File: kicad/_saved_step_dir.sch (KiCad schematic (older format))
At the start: 17 parts, among them J1001 tblock2x6, U1001 am26ls32a

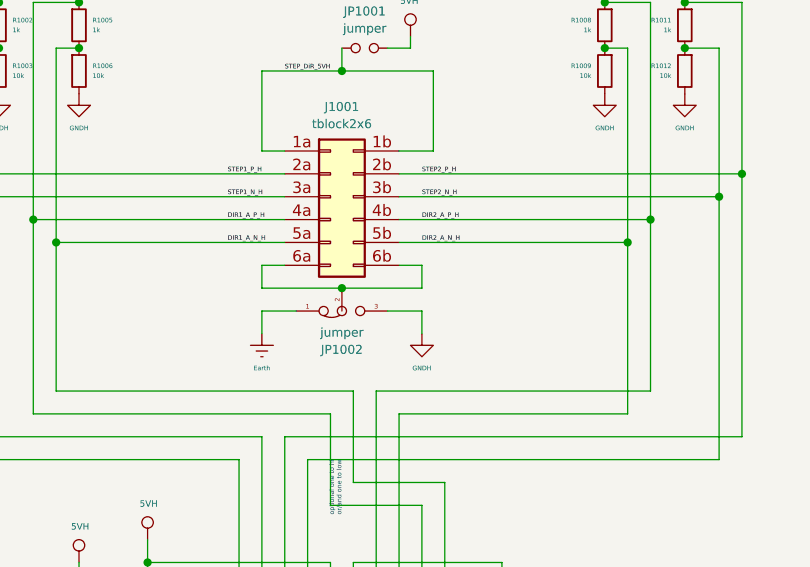
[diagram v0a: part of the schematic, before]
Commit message: roouting and more routing.... I think 4 layers WONT be enought
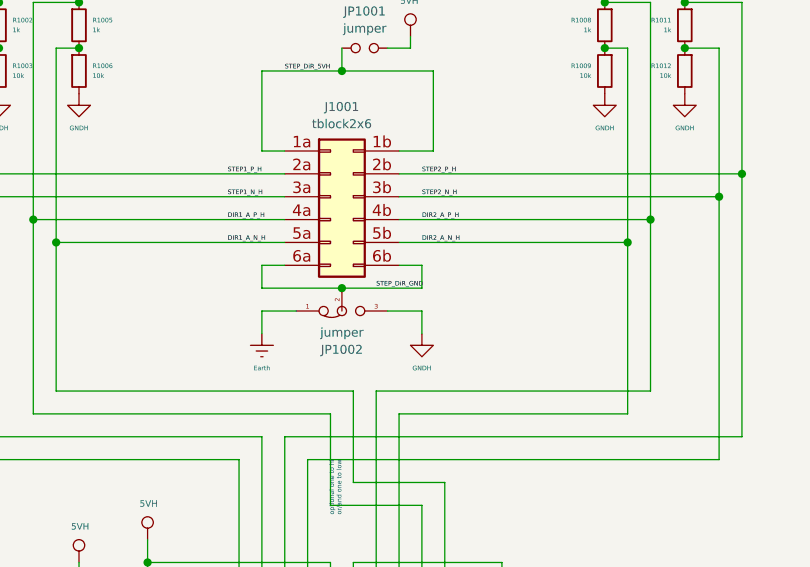
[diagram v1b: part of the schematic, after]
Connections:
- net STEP_DiR_GND: now reaches J1001.6a (Pin_6a), J1001.6b (Pin_6b), JP1002.2 (C)
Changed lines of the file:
@@
 Text Label 8400 3300 0    20   ~ 0
 STEP_DiR_5VH
+Text Label 8800 4250 0    20   ~ 0
+STEP_DiR_GND
 $EndSCHEMATC
